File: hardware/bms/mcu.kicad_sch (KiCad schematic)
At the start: 75 parts, among them J9 Micro_SD_Card_Det2, SW2 SW_Push, SW3 SW_Push, U4 LM5166X, U5 TPS62172DSG, U6 ESP32-C3-MINI-1-N4, U9 TXU0101DCKR

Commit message: Swapped out SD card holder to a push-push version, should be nicer. Also a lot of routing and power plane work
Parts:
- J9: footprint bms:microSD_HC_Molex_104031-0811 -> bms:MOLEX_503398-1892; MFG PN 1040310811 -> 5033981892
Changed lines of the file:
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@@
       (effects (font (size 1.27 1.27)) hide)
     )
-    (property "Footprint" "bms:microSD_HC_Molex_104031-0811" (at 309.88 105.41 0)
+    (property "Footprint" "bms:MOLEX_503398-1892" (at 309.88 105.41 0)
       (effects (font (size 1.27 1.27)) hide)
     )
-    (property "Datasheet" "https://tools.molex.com/pdm_docs/sd/1040310811_sd.pdf" (at 260.35 120.65 0)
+    (property "Datasheet" "https://tools.molex.com/pdm_docs/sd/5033981892_sd.pdf" (at 260.35 120.65 0)
       (effects (font (size 1.27 1.27)) hide)
     )
@@
       (effects (font (size 1.27 1.27)) hide)
     )
-    (property "MFG PN" "1040310811" (at 257.81 123.19 0)
+    (property "MFG PN" "5033981892" (at 257.81 123.19 0)
       (effects (font (size 1.27 1.27)) hide)
     )

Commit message: Review of BMS board looks good, finished!
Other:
- note added: "To further reduce the chance of corruption, SD card writes will only occur evey ~10-15s."
- moved on the sheet: D?
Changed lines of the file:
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@@
-    (stroke (width 0) (type default))
-  )
-  (wire (pts (xy 64.77 26.67) (xy 91.44 26.67))
     (stroke (width 0) (type default))
   )
@@
     (stroke (width 0) (type default))
   )
+  (wire (pts (xy 50.8 25.4) (xy 91.44 25.4))
+    (stroke (width 0) (type default))
+  )
   (wire (pts (xy 175.26 105.41) (xy 184.15 105.41))
     (stroke (width 0) (type default))
@@
     (stroke (width 0) (type default))
   )
-  (wire (pts (xy 64.77 30.48) (xy 73.66 30.48))
+  (wire (pts (xy 50.8 30.48) (xy 73.66 30.48))
     (stroke (width 0) (type default))
   )
@@
     (stroke (width 0) (type default))
   )
-  (wire (pts (xy 120.65 26.67) (xy 120.65 43.18))
+  (wire (pts (xy 120.65 25.4) (xy 120.65 43.18))
     (stroke (width 0) (type default))
   )
@@
     (stroke (width 0) (type default))
   )
-  (wire (pts (xy 99.06 26.67) (xy 120.65 26.67))
+  (wire (pts (xy 99.06 25.4) (xy 120.65 25.4))
     (stroke (width 0) (type default))
   )
@@
     (effects (font (size 1.27 1.27)) (justify left bottom))
   )
+  (text "To further reduce the chance of corruption, \nSD card writes will only occur evey ~10-15s."
+    (at 25.4 78.74 0)
+    (effects (font (size 1.27 1.27)) (justify left bottom))
+  )
   (text "eSUP BMS - MCU" (at 187.96 176.53 0)
     (effects (font (size 3.81 3.81) (thickness 0.762) bold italic) (justify left bottom))
@@
     (effects (font (size 1.27 1.27)) (justify left bottom))
   )
-  (label "USB_VIN" (at 68.58 26.67 0) (fields_autoplaced)
+  (label "USB_VIN" (at 68.58 25.4 0) (fields_autoplaced)
     (effects (font (size 1.27 1.27)) (justify left bottom))
   )
@@
     (effects (font (size 1.27 1.27)) (justify right))
   )
-  (hierarchical_label "MCU_VIN" (shape input) (at 64.77 30.48 180) (fields_autoplaced)
+  (hierarchical_label "MCU_VIN" (shape input) (at 50.8 30.48 180) (fields_autoplaced)
     (effects (font (size 1.27 1.27)) (justify right))
   )
@@
     (effects (font (size 1.27 1.27)) (justify right))
   )
-  (hierarchical_label "USB_VIN" (shape input) (at 64.77 26.67 180) (fields_autoplaced)
+  (hierarchical_label "USB_VIN" (shape input) (at 50.8 25.4 180) (fields_autoplaced)
     (effects (font (size 1.27 1.27)) (justify right))
   )
@@
     )
   )
-  (symbol (lib_id "Device:D_Schottky") (at 95.25 26.67 180) (unit 1)
-    (in_bom yes) (on_board yes) (dnp no)
-    (property "Reference" "D?" (at 95.25 24.13 0)
-      (effects (font (size 1.27 1.27)))
-    )
-    (property "Value" "D_Schottky" (at 96.393 24.638 90)
+  (symbol (lib_id "Device:D_Schottky") (at 95.25 25.4 180) (unit 1)
+    (in_bom yes) (on_board yes) (dnp no)
+    (property "Reference" "D?" (at 95.25 22.86 0)
+      (effects (font (size 1.27 1.27)))
+    )
+    (property "Value" "D_Schottky" (at 96.393 23.368 90)
       (effects (font (size 1.27 1.27)) (justify right) hide)
     )
-    (property "Footprint" "Diode_SMD:D_SOD-123" (at 95.25 26.67 0)
-      (effects (font (size 1.27 1.27)) hide)
-    )
-    (property "Datasheet" "~" (at 95.25 26.67 0)
-      (effects (font (size 1.27 1.27)) hide)
-    )
-    (property "Voltage" "40V" (at 95.25 29.21 0)
-      (effects (font (size 1.27 1.27)))
-    )
-    (property "MFG" "Diodes Incorporated" (at 95.25 26.67 0)
-      (effects (font (size 1.27 1.27)) hide)
-    )
-    (property "MFG PN" "1N5819HW-7-F" (at 95.25 26.67 0)
-      (effects (font (size 1.27 1.27)) hide)
-    )
-    (property "Current Rating" "1A" (at 95.25 26.67 0)
-      (effects (font (size 1.27 1.27)) hide)
-    )
-    (property "VF" "450mV" (at 95.25 26.67 0)
-      (effects (font (size 1.27 1.27)) hide)
-    )
+    (property "Footprint" "Diode_SMD:D_SOD-123" (at 95.25 25.4 0)
+      (effects (font (size 1.27 1.27)) hide)
+    )
+    (property "Datasheet" "~" (at 95.25 25.4 0)
+      (effects (font (size 1.27 1.27)) hide)
+    )
+    (property "Voltage" "40V" (at 95.25 27.94 0)
+      (effects (font (size 1.27 1.27)))
+    )
+    (property "MFG" "Diodes Incorporated" (at 95.25 25.4 0)
+      (effects (font (size 1.27 1.27)) hide)
+    )
+    (property "MFG PN" "1N5819HW-7-F" (at 95.25 25.4 0)
+      (effects (font (size 1.27 1.27)) hide)
+    )
+    (property "Current Rating" "1A" (at 95.25 25.4 0)
+      (effects (font (size 1.27 1.27)) hide)
+    )
+    (property "VF" "450mV" (at 95.25 25.4 0)
+      (effects (font (size 1.27 1.27)) hide)
+    )

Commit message: Exported gerbers for both boards
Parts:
- U4: footprint Package_SON:Texas_S-PVSON-N10_ThermalVias -> bms:Texas_S-PVSON-N10_ThermalVias
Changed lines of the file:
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@@
       (effects (font (size 1.27 1.27)))
     )
-    (property "Footprint" "Package_SON:Texas_S-PVSON-N10_ThermalVias" (at 95.25 62.23 0)
+    (property "Footprint" "bms:Texas_S-PVSON-N10_ThermalVias" (at 95.25 62.23 0)
       (effects (font (size 1.27 1.27)) (justify left) hide)
     )

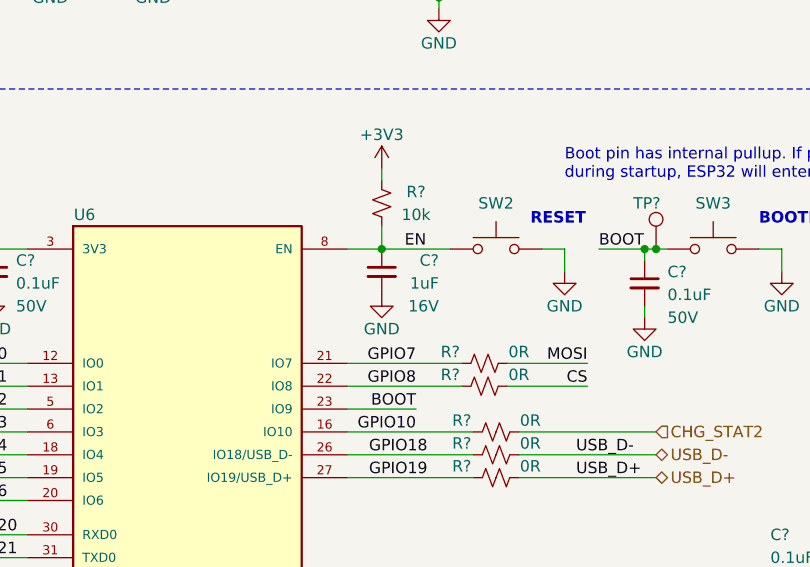
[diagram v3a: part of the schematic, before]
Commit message: Updated MFG PNs, BOM ordered.
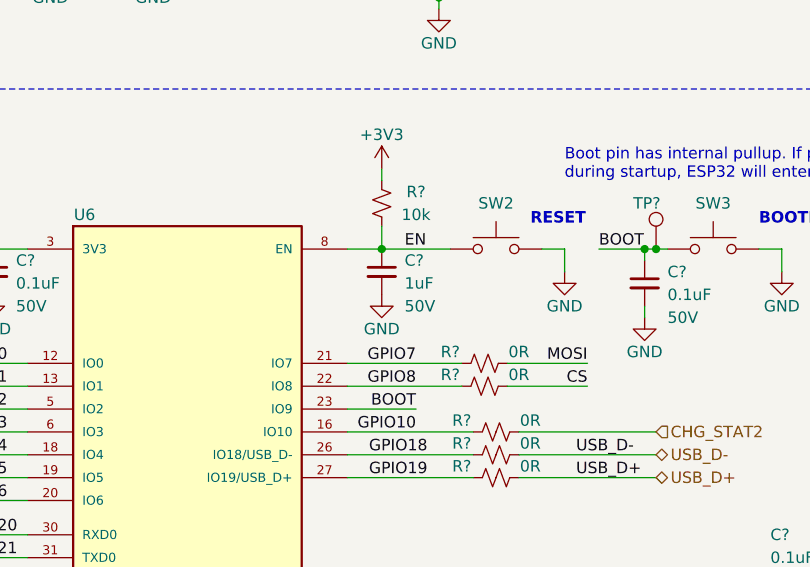
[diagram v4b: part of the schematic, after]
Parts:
- removed C?: 1uF, Capacitor_SMD:C_0603_1608Metric, symbol Device:C_Small
- added C?: 1uF, Capacitor_SMD:C_0603_1608Metric, symbol Device:C_Small
- D19: MFG (none) -> Adafruit; MFG PN (none) -> 4684
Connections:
- net EN: now also C?.1
- net GND: now also C?.2
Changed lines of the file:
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@@
-    )
-  )
-  (symbol (lib_id "Device:C_Small") (at 161.29 92.71 0) (mirror y) (unit 1)
-    (in_bom yes) (on_board yes) (dnp no)
-    (property "Reference" "C?" (at 167.64 91.44 0)
-      (effects (font (size 1.27 1.27)) (justify left))
-    )
-    (property "Value" "1uF" (at 167.64 93.98 0)
-      (effects (font (size 1.27 1.27)) (justify left))
-    )
-    (property "Footprint" "Capacitor_SMD:C_0603_1608Metric" (at 161.29 92.71 0)
-      (effects (font (size 1.27 1.27)) hide)
-    )
-    (property "Datasheet" "~" (at 161.29 92.71 0)
-      (effects (font (size 1.27 1.27)) hide)
-    )
-    (property "MFG" "Murata Electronics" (at 161.29 92.71 0)
-      (effects (font (size 1.27 1.27)) hide)
-    )
-    (property "MFG PN" "GCM188R71C105KA64J" (at 161.29 92.71 0)
-      (effects (font (size 1.27 1.27)) hide)
-    )
-    (property "Voltage" "16V" (at 167.64 96.52 0)
-      (effects (font (size 1.27 1.27)) (justify left))
-    )
-    (pin "1")
-    (pin "2")
-    (instances
-      (project "bms"
-        (path "/a4805e9d-b940-444e-a7cb-db4f4c53ed46/00000000-0000-0000-0000-00006523a805"
-          (reference "C?") (unit 1)
-        )
-        (path "/a4805e9d-b940-444e-a7cb-db4f4c53ed46/00000000-0000-0000-0000-00006523ab32"
-          (reference "C?") (unit 1)
-        )
-        (path "/a4805e9d-b940-444e-a7cb-db4f4c53ed46/00000000-0000-0000-0000-00006658c265"
-          (reference "C66") (unit 1)
-        )
-      )
     )
   )
@@
       (effects (font (size 1.27 1.27)) (justify left top) hide)
     )
+    (property "MFG" "Adafruit" (at 85.09 173.99 0)
+      (effects (font (size 1.27 1.27)) hide)
+    )
+    (property "MFG PN" "4684" (at 85.09 173.99 0)
+      (effects (font (size 1.27 1.27)) hide)
+    )
     (pin "1")
     (pin "2")
@@
         )
       )
+    )
+  )
+  (symbol (lib_id "Device:C_Small") (at 161.29 92.71 0) (unit 1)
+    (in_bom yes) (on_board yes) (dnp no)
+    (property "Reference" "C?" (at 163.83 91.44 0)
+      (effects (font (size 1.27 1.27)) (justify left))
+    )
+    (property "Value" "1uF" (at 163.83 93.98 0)
+      (effects (font (size 1.27 1.27)) (justify left))
+    )
+    (property "Footprint" "Capacitor_SMD:C_0603_1608Metric" (at 161.29 92.71 0)
+      (effects (font (size 1.27 1.27)) hide)
+    )
+    (property "Datasheet" "~" (at 161.29 92.71 0)
+      (effects (font (size 1.27 1.27)) hide)
+    )
+    (property "MFG" "Murata Electronics" (at 161.29 92.71 0)
+      (effects (font (size 1.27 1.27)) hide)
+    )
+    (property "MFG PN" "GRT188R61H105KE13D" (at 161.29 92.71 0)
+      (effects (font (size 1.27 1.27)) hide)
+    )
+    (property "Voltage" "50V" (at 163.83 96.52 0)
+      (effects (font (size 1.27 1.27)) (justify left))
+    )
+    (pin "1")
+    (pin "2")
+    (instances
+      (project "bms"
+        (path "/a4805e9d-b940-444e-a7cb-db4f4c53ed46/00000000-0000-0000-0000-00006523a805"
+          (reference "C?") (unit 1)
+        )
+        (path "/a4805e9d-b940-444e-a7cb-db4f4c53ed46/00000000-0000-0000-0000-00006523ab32"
+          (reference "C47") (unit 1)
+        )
+        (path "/a4805e9d-b940-444e-a7cb-db4f4c53ed46/00000000-0000-0000-0000-00006658c265"
+          (reference "C66") (unit 1)
+        )
+      )
